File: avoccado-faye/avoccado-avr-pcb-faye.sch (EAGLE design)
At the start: 53 parts, among them Q1 16MHz, Q2 FET, U2 MCP73831

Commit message: rerouting bottom half
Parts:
- added JP1, JP7: M01NOSILK-KIT, SparkFun-Connectors:M01NOSILK-KIT
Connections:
- removed net N$3: C7.1, R7.2, R8.1
- net A3: now also C7.1, R7.2, R8.1
- net GND: now also JP7.1
- net VBAT: now also JP1.1
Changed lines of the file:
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@@
 <part name="C7" library="SparkFun" deviceset="CAP" device="0402" value="0.1uF"/>
 <part name="GND10" library="SparkFun" deviceset="GND" device=""/>
+<part name="JP1" library="SparkFun-Connectors" deviceset="M01" device="NOSILK-KIT" value="M01NOSILK-KIT"/>
+<part name="JP7" library="SparkFun-Connectors" deviceset="M01" device="NOSILK-KIT" value="M01NOSILK-KIT"/>
 </parts>
 <sheets>
@@
 <instance part="C7" gate="G$1" x="30.48" y="25.4"/>
 <instance part="GND10" gate="1" x="20.32" y="12.7"/>
+<instance part="JP1" gate="G$1" x="383.54" y="-17.78" rot="R180"/>
+<instance part="JP7" gate="G$1" x="383.54" y="-7.62" rot="R180"/>
 </instances>
 <busses>
@@
 <wire x1="30.48" y1="17.78" x2="20.32" y2="17.78" width="0.1524" layer="91"/>
 <junction x="20.32" y="17.78"/>
+</segment>
+<segment>
+<wire x1="375.92" y1="-7.62" x2="350.52" y2="-7.62" width="0.1524" layer="91"/>
+<pinref part="JP7" gate="G$1" pin="1"/>
+<label x="350.52" y="-7.62" size="1.778" layer="95"/>
 </segment>
 </net>
@@
 <label x="340.36" y="154.94" size="1.778" layer="95"/>
 </segment>
+<segment>
+<pinref part="R7" gate="G$1" pin="2"/>
+<pinref part="R8" gate="G$1" pin="1"/>
+<wire x1="20.32" y1="30.48" x2="20.32" y2="33.02" width="0.1524" layer="91"/>
+<pinref part="C7" gate="G$1" pin="1"/>
+<wire x1="20.32" y1="33.02" x2="20.32" y2="35.56" width="0.1524" layer="91"/>
+<wire x1="30.48" y1="30.48" x2="30.48" y2="33.02" width="0.1524" layer="91"/>
+<wire x1="30.48" y1="33.02" x2="20.32" y2="33.02" width="0.1524" layer="91"/>
+<junction x="20.32" y="33.02"/>
+<wire x1="55.88" y1="33.02" x2="30.48" y2="33.02" width="0.1524" layer="91"/>
+<junction x="30.48" y="33.02"/>
+</segment>
 </net>
 <net name="A2" class="0">
@@
 <label x="17.78" y="53.34" size="1.778" layer="95" rot="R90"/>
 <pinref part="R8" gate="G$1" pin="2"/>
+</segment>
+<segment>
+<wire x1="375.92" y1="-17.78" x2="350.52" y2="-17.78" width="0.1524" layer="91"/>
+<pinref part="JP1" gate="G$1" pin="1"/>
+<label x="350.52" y="-17.78" size="1.778" layer="95"/>
 </segment>
 </net>
@@
 </segment>
 </net>
-<net name="N$3" class="0">
-<segment>
-<pinref part="R7" gate="G$1" pin="2"/>
-<pinref part="R8" gate="G$1" pin="1"/>
-<wire x1="20.32" y1="30.48" x2="20.32" y2="33.02" width="0.1524" layer="91"/>
-<pinref part="C7" gate="G$1" pin="1"/>
-<wire x1="20.32" y1="33.02" x2="20.32" y2="35.56" width="0.1524" layer="91"/>
-<wire x1="30.48" y1="30.48" x2="30.48" y2="33.02" width="0.1524" layer="91"/>
-<wire x1="30.48" y1="33.02" x2="20.32" y2="33.02" width="0.1524" layer="91"/>
-<junction x="20.32" y="33.02"/>
-</segment>
-</net>

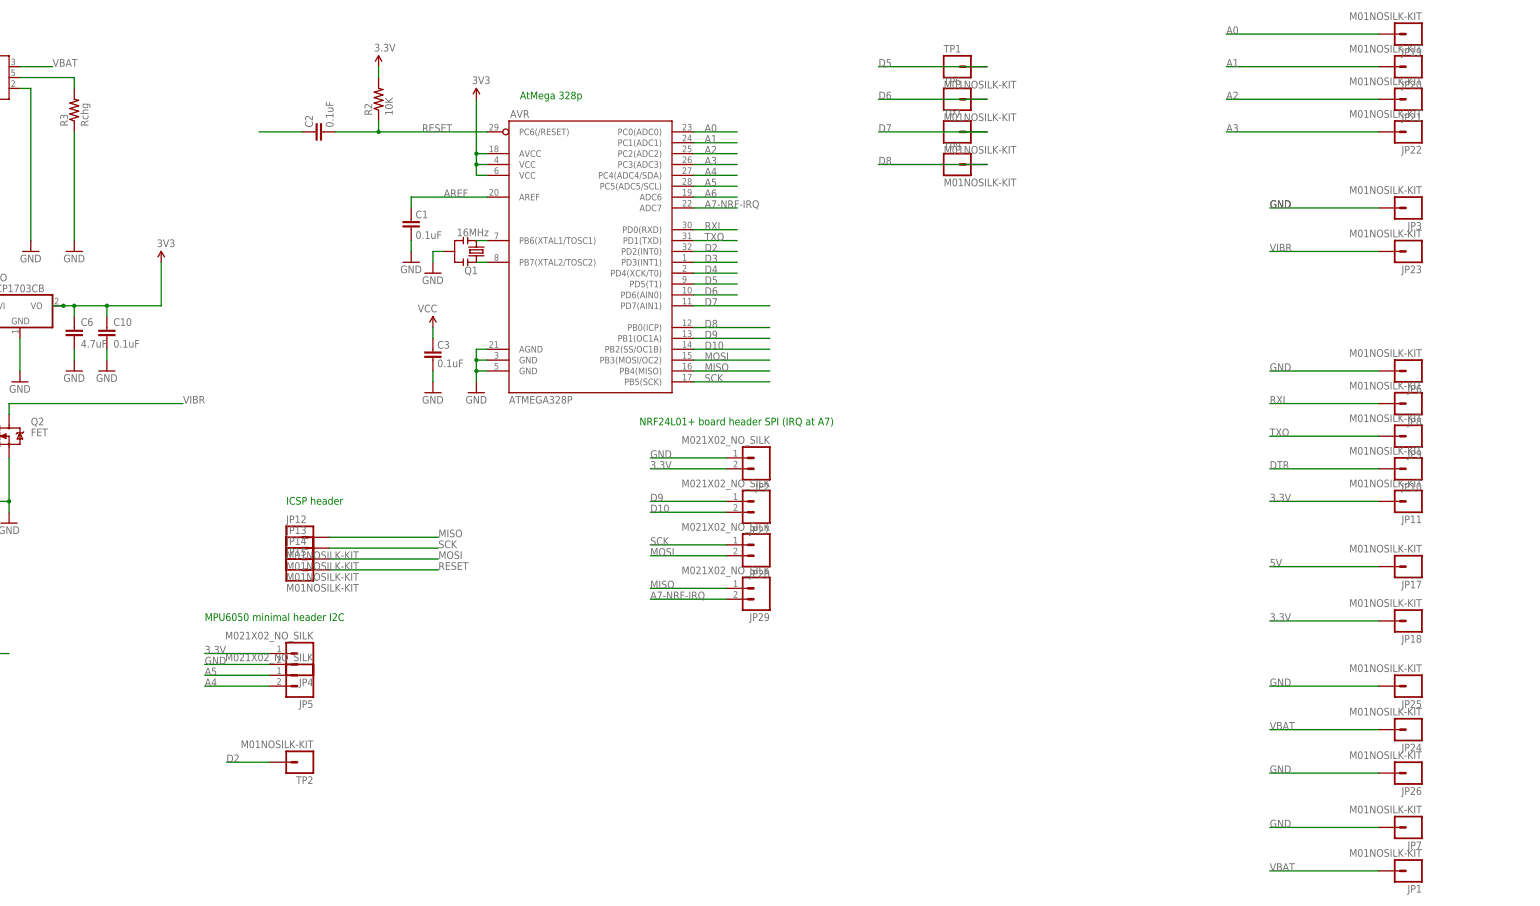
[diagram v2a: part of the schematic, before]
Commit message: all signals routed to spec
TODO: snap to grid, silkscreen
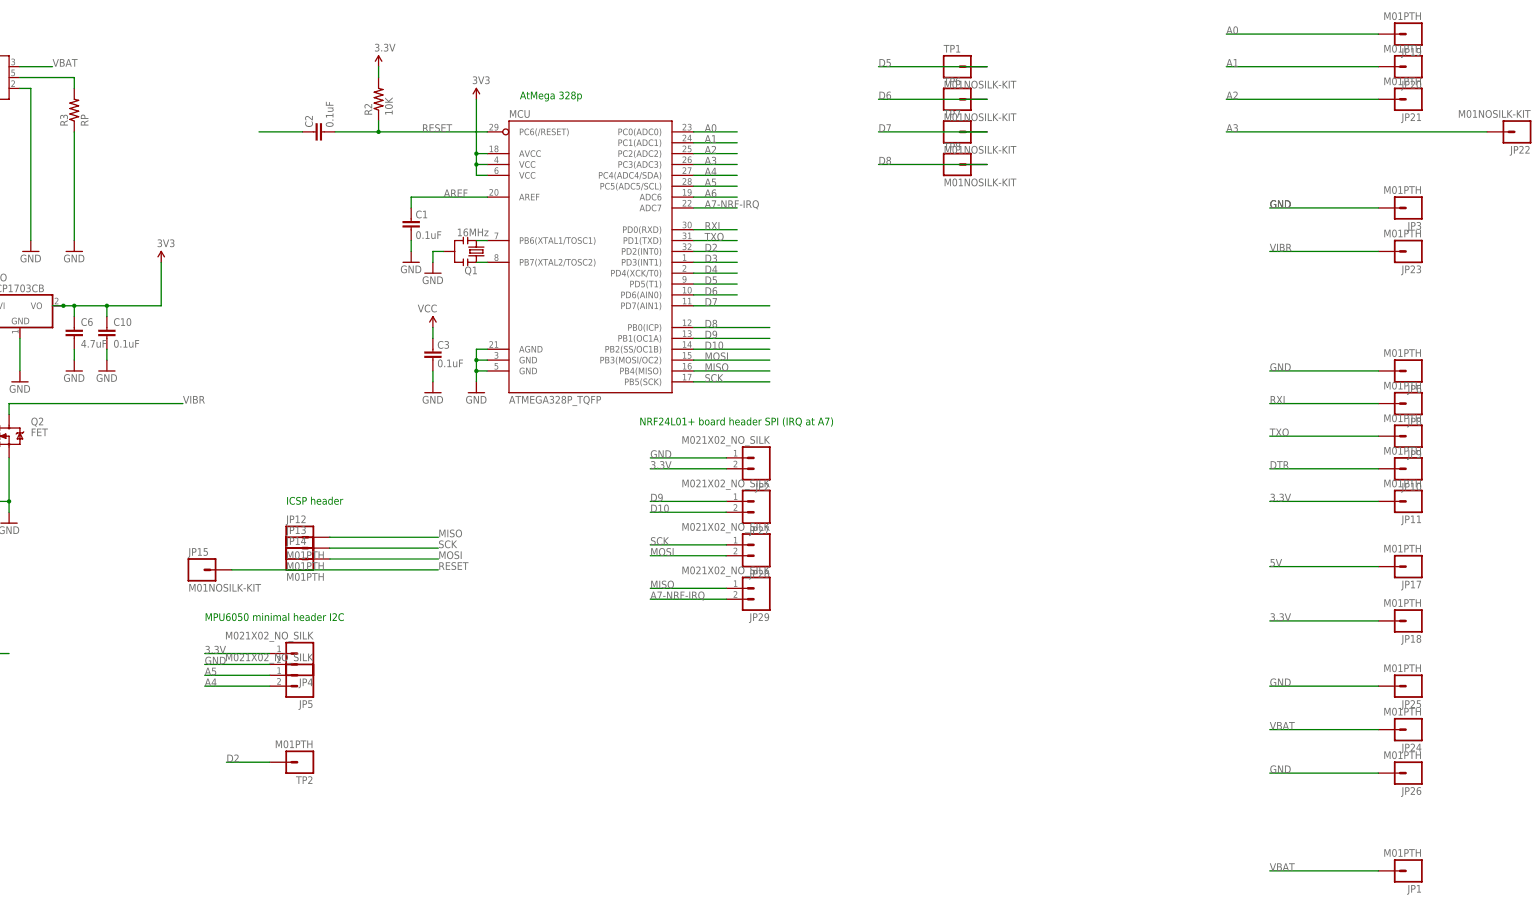
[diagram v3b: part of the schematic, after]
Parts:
- removed AVR: ATMEGA328P, SparkFun-DigitalIC:ATMEGA328_SMT
- removed JP7: M01NOSILK-KIT, SparkFun-Connectors:M01NOSILK-KIT
- added MCU: ATMEGA328P_TQFP, SparkFun-DigitalIC:ATMEGA328P_TQFP
- JP1, JP10, JP11, JP12, JP13, JP14, JP17, JP18, JP19, JP20, JP21, JP23, JP24, JP25, JP26, JP3, JP6, JP8, JP9, TP2: value M01NOSILK-KIT -> M01PTH; device SparkFun-Connectors:M01NOSILK-KIT -> SparkFun-Connectors:M01PTH
- R3: value Rchg -> RP
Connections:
- net 3.3V: now also MCU.AVCC, MCU.VCC@4, MCU.VCC@6; no longer AVR.AVCC, AVR.VCC@1, AVR.VCC@2
- net A0: now also MCU.PC0(ADC0); no longer AVR.PC0(ADC0)
- net A1: now also MCU.PC1(ADC1); no longer AVR.PC1(ADC1)
- net A2: now also MCU.PC2(ADC2); no longer AVR.PC2(ADC2)
- net A3: now also MCU.PC3(ADC3); no longer AVR.PC3(ADC3)
- net A4: now also MCU.PC4(ADC4/SDA); no longer AVR.PC4(ADC4/SDA)
- net A5: now also MCU.PC5(ADC5/SCL); no longer AVR.PC5(ADC5/SCL)
- net A6: now also MCU.ADC6; no longer AVR.ADC6
- net A7-NRF-IRQ: now also MCU.ADC7; no longer AVR.ADC7
- net AREF: now also MCU.AREF; no longer AVR.AREF
- net D10: now also MCU.PB2(SS/OC1B); no longer AVR.PB2(SS/OC1B)
- net D2: now also MCU.PD2(INT0); no longer AVR.PD2(INT0)
- net D3: now also MCU.PD3(INT1); no longer AVR.PD3(INT1)
- net D4: now also MCU.PD4(XCK/T0); no longer AVR.PD4(XCK/T0)
- net D5: now also MCU.PD5(T1); no longer AVR.PD5(T1)
- net D6: now also MCU.PD6(AIN0); no longer AVR.PD6(AIN0)
- net D7: now also MCU.PD7(AIN1); no longer AVR.PD7(AIN1)
- net D8: now also MCU.PB0(ICP); no longer AVR.PB0(ICP)
- net D9: now also MCU.PB1(OC1A); no longer AVR.PB1(OC1A)
- net GND: now also MCU.AGND, MCU.GND@3, MCU.GND@5; no longer AVR.AGND, AVR.GND@1, AVR.GND@2, JP7.1
- net MISO: now also MCU.PB4(MISO); no longer AVR.PB4(MISO)
- net MOSI: now also MCU.PB3(MOSI/OC2); no longer AVR.PB3(MOSI/OC2)
- net N$1: now also MCU.PB7(XTAL2/TOSC2); no longer AVR.PB7(XTAL2/TOSC2)
- net N$2: now also MCU.PB6(XTAL1/TOSC1); no longer AVR.PB6(XTAL1/TOSC1)
- net RESET: now also MCU.PC6(/RESET); no longer AVR.PC6(/RESET)
- net RXI: now also MCU.PD0(RXD); no longer AVR.PD0(RXD)
- net SCK: now also MCU.PB5(SCK); no longer AVR.PB5(SCK)
- net TXO: now also MCU.PD1(TXD); no longer AVR.PD1(TXD)
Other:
- moved on the sheet: JP15, JP22

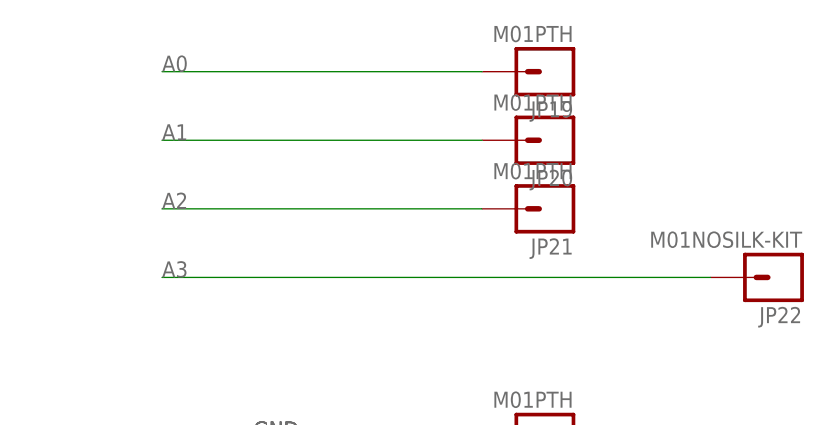
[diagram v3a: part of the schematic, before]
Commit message: change footprint of mosfet to sot23-3
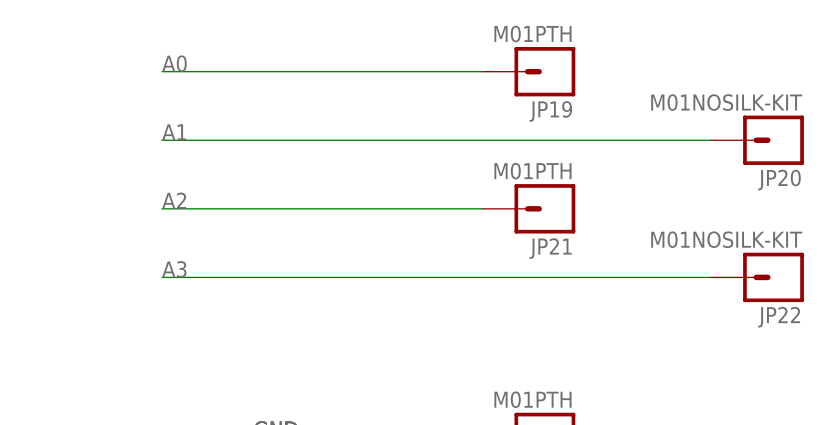
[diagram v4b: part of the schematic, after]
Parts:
- JP20: value M01PTH -> M01NOSILK-KIT; device SparkFun-Connectors:M01PTH -> SparkFun-Connectors:M01NOSILK-KIT
- Q2: device SparkFun-DiscreteSemi:MOSFET-NCHANNEL2N7002PW -> SparkFun-DiscreteSemi:MOSFET-NCHANNELBSS123LT1G
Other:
- moved on the sheet: JP20
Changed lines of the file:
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@@
 <part name="P+1" library="SparkFun" deviceset="3.3V" device="" value="3V3"/>
 <part name="GND5" library="SparkFun" deviceset="GND" device=""/>
-<part name="Q2" library="SparkFun-DiscreteSemi" deviceset="MOSFET-NCHANNEL" device="2N7002PW" value="FET"/>
+<part name="Q2" library="SparkFun-DiscreteSemi" deviceset="MOSFET-NCHANNEL" device="BSS123LT1G" value="FET"/>
 <part name="R1" library="SparkFun-Resistors" deviceset="RESISTOR" device="0603" value="1K"/>
 <part name="LDO" library="linear" deviceset="MCP1703" device="CB"/>
@@
 <part name="TP8" library="SparkFun-Connectors" deviceset="M01" device="NOSILK-KIT"/>
 <part name="JP19" library="SparkFun-Connectors" deviceset="M01" device="PTH" value="M01PTH"/>
-<part name="JP20" library="SparkFun-Connectors" deviceset="M01" device="PTH" value="M01PTH"/>
+<part name="JP20" library="SparkFun-Connectors" deviceset="M01" device="NOSILK-KIT" value="M01NOSILK-KIT"/>
 <part name="JP21" library="SparkFun-Connectors" deviceset="M01" device="PTH" value="M01PTH"/>
 <part name="JP22" library="SparkFun-Connectors" deviceset="M01" device="NOSILK-KIT" value="M01NOSILK-KIT"/>
@@
 <instance part="TP8" gate="G$1" x="276.86" y="147.32"/>
 <instance part="JP19" gate="G$1" x="383.54" y="177.8" rot="R180"/>
-<instance part="JP20" gate="G$1" x="383.54" y="170.18" rot="R180"/>
+<instance part="JP20" gate="G$1" x="408.94" y="170.18" rot="R180"/>
 <instance part="JP21" gate="G$1" x="383.54" y="162.56" rot="R180"/>
 <instance part="JP22" gate="G$1" x="408.94" y="154.94" rot="R180"/>
@@
 </segment>
 <segment>
-<wire x1="340.36" y1="170.18" x2="375.92" y2="170.18" width="0.1524" layer="91"/>
+<wire x1="340.36" y1="170.18" x2="401.32" y2="170.18" width="0.1524" layer="91"/>
 <pinref part="JP20" gate="G$1" pin="1"/>
 <label x="340.36" y="170.18" size="1.778" layer="95"/>

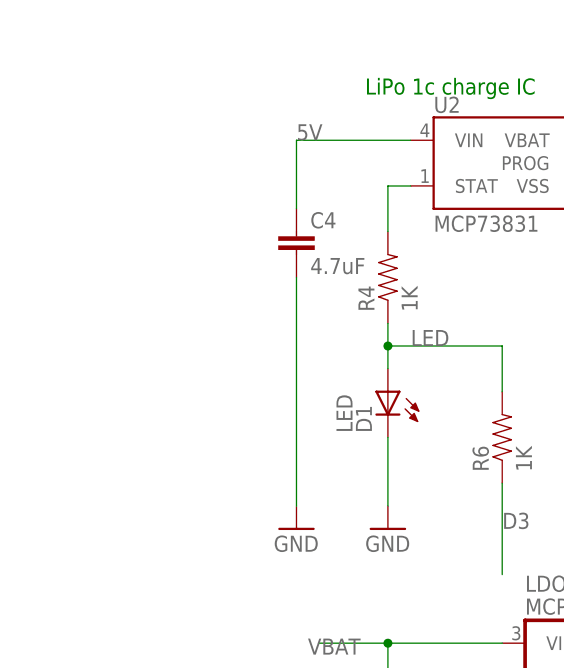
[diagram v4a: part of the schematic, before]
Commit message: micro usb on the bottom
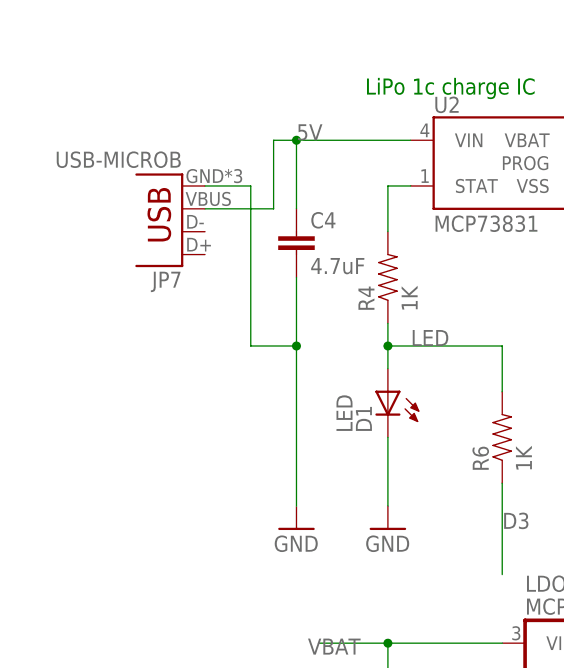
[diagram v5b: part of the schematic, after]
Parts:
- added JP7: USB-MICROB, SparkFun-Connectors:USB-MICROB
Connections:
- net 5V: now also JP7.VBUS
- net GND: now also JP7.GND
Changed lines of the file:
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@@
 <part name="JP1" library="SparkFun-Connectors" deviceset="M01" device="PTH" value="M01PTH"/>
 <part name="MCU" library="SparkFun-DigitalIC" deviceset="ATMEGA328P_TQFP" device="" value="ATMEGA328P_TQFP"/>
+<part name="JP7" library="SparkFun-Connectors" deviceset="USB" device="-MICROB"/>
 </parts>
 <sheets>
@@
 <instance part="JP1" gate="G$1" x="383.54" y="-17.78" rot="R180"/>
 <instance part="MCU" gate="U$1" x="193.04" y="124.46"/>
+<instance part="JP7" gate="G$1" x="12.7" y="165.1" rot="R180"/>
 </instances>
 <busses>
@@
 <pinref part="C4" gate="G$1" pin="2"/>
 <pinref part="GND8" gate="1" pin="GND"/>
-<wire x1="25.4" y1="154.94" x2="25.4" y2="129.54" width="0.1524" layer="91"/>
+<wire x1="25.4" y1="154.94" x2="25.4" y2="147.32" width="0.1524" layer="91"/>
+<pinref part="JP7" gate="G$1" pin="GND"/>
+<wire x1="25.4" y1="147.32" x2="25.4" y2="129.54" width="0.1524" layer="91"/>
+<wire x1="15.24" y1="165.1" x2="20.32" y2="165.1" width="0.1524" layer="91"/>
+<wire x1="20.32" y1="165.1" x2="20.32" y2="147.32" width="0.1524" layer="91"/>
+<wire x1="20.32" y1="147.32" x2="25.4" y2="147.32" width="0.1524" layer="91"/>
+<junction x="25.4" y="147.32"/>
 </segment>
 <segment>
@@
 <wire x1="25.4" y1="170.18" x2="25.4" y2="162.56" width="0.1524" layer="91"/>
 <label x="25.4" y="170.18" size="1.778" layer="95"/>
-</segment>
-<segment>
+<pinref part="JP7" gate="G$1" pin="VBUS"/>
+<wire x1="15.24" y1="162.56" x2="22.86" y2="162.56" width="0.1524" layer="91"/>
+<wire x1="22.86" y1="162.56" x2="22.86" y2="170.18" width="0.1524" layer="91"/>
+<wire x1="22.86" y1="170.18" x2="25.4" y2="170.18" width="0.1524" layer="91"/>
+<junction x="25.4" y="170.18"/>
+</segment>
+<segment>

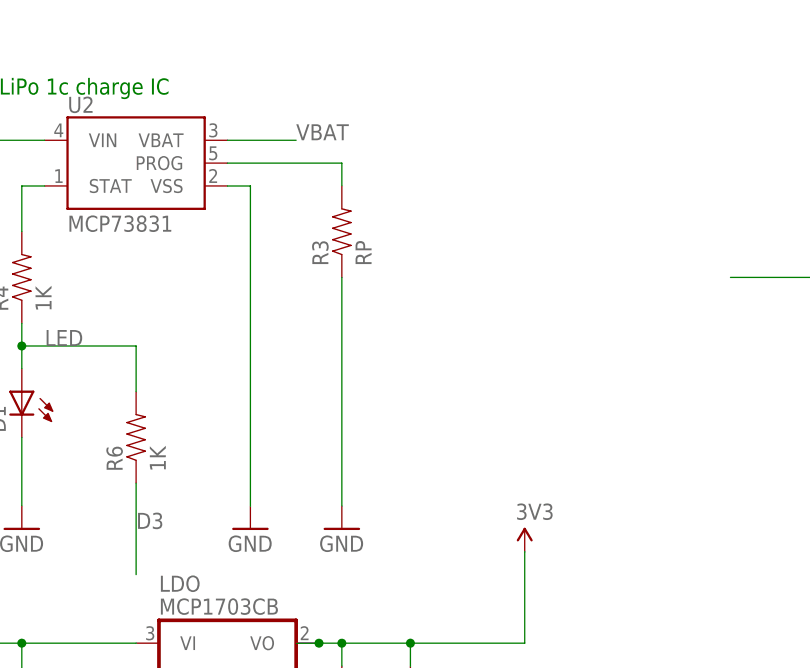
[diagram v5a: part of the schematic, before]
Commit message: route USB connector, additional headers
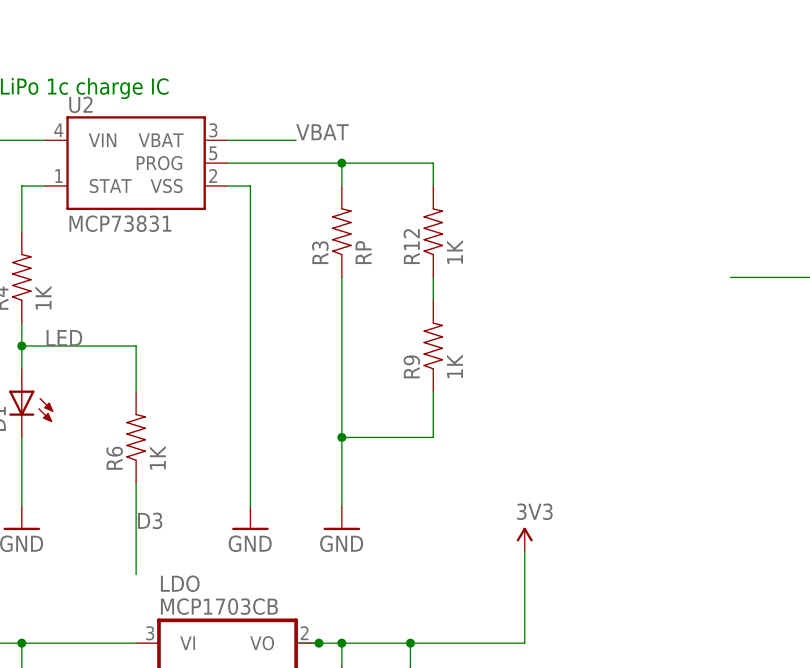
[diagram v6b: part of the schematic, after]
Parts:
- added R12, R9: 1K, SparkFun-Resistors:RESISTOR0402
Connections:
- new net N$3: R12.1, R9.2
- net CHG-PROG: now also R12.2
- net GND: now also R9.1
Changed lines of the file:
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@@
 <part name="MCU" library="SparkFun-DigitalIC" deviceset="ATMEGA328P_TQFP" device="" value="ATMEGA328P_TQFP"/>
 <part name="JP7" library="SparkFun-Connectors" deviceset="USB" device="-MICROB"/>
+<part name="R12" library="SparkFun-Resistors" deviceset="RESISTOR" device="0402" value="1K"/>
+<part name="R9" library="SparkFun-Resistors" deviceset="RESISTOR" device="0402" value="1K"/>
 </parts>
 <sheets>
@@
 <instance part="MCU" gate="U$1" x="193.04" y="124.46"/>
 <instance part="JP7" gate="G$1" x="12.7" y="165.1" rot="R180"/>
+<instance part="R12" gate="G$1" x="81.28" y="160.02" rot="R90"/>
+<instance part="R9" gate="G$1" x="81.28" y="147.32" rot="R90"/>
 </instances>
 <busses>
@@
 <pinref part="R3" gate="G$1" pin="1"/>
 <pinref part="GND3" gate="1" pin="GND"/>
-<wire x1="71.12" y1="154.94" x2="71.12" y2="129.54" width="0.1524" layer="91"/>
+<wire x1="71.12" y1="154.94" x2="71.12" y2="137.16" width="0.1524" layer="91"/>
+<pinref part="R9" gate="G$1" pin="1"/>
+<wire x1="71.12" y1="137.16" x2="71.12" y2="129.54" width="0.1524" layer="91"/>
+<wire x1="81.28" y1="142.24" x2="81.28" y2="137.16" width="0.1524" layer="91"/>
+<wire x1="81.28" y1="137.16" x2="71.12" y2="137.16" width="0.1524" layer="91"/>
+<junction x="71.12" y="137.16"/>
 </segment>
 <segment>
@@
 <pinref part="U2" gate="G$1" pin="PROG"/>
 <wire x1="71.12" y1="167.64" x2="58.42" y2="167.64" width="0.1524" layer="91"/>
+<pinref part="R12" gate="G$1" pin="2"/>
+<wire x1="71.12" y1="167.64" x2="81.28" y2="167.64" width="0.1524" layer="91"/>
+<wire x1="81.28" y1="167.64" x2="81.28" y2="165.1" width="0.1524" layer="91"/>
+<junction x="71.12" y="167.64"/>
 </segment>
 </net>
@@
 </segment>
 </net>
+<net name="N$3" class="0">
+<segment>
+<pinref part="R12" gate="G$1" pin="1"/>
+<pinref part="R9" gate="G$1" pin="2"/>
+<wire x1="81.28" y1="154.94" x2="81.28" y2="152.4" width="0.1524" layer="91"/>
+</segment>
+</net>
